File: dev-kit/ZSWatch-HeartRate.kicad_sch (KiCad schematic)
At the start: 49 parts, among them IC101 LIS2DS12, IC102 MCP73832-2-OT, IC103 MAX32664, IC104 TPS61240, IC105 MAX86141, IC106 MIC5365-1.8, J101 SPI, J102 GPIO, J103 UART, J104 I2C, M101 BM15C, SW101 BTN1, SW102 RESET, X102 CHARGE, X103 BATTERY, X104 DEBUG, Y101 32kHz

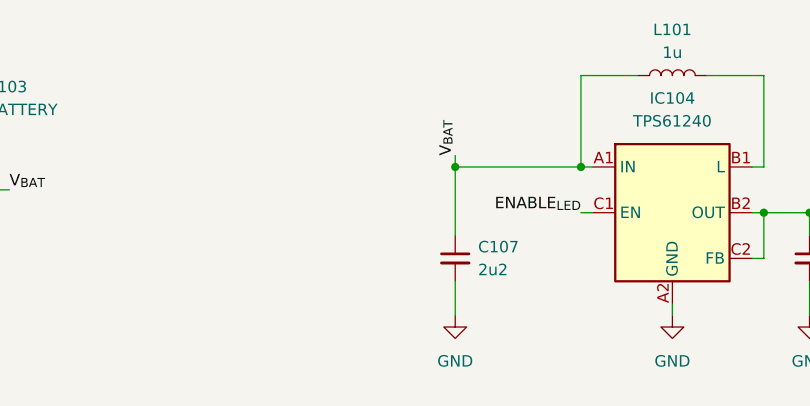
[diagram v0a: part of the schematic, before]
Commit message: Start with hardware rev 3
- Fix distance between programming and battery connector

Signed-off-by: Daniel Kampert <DanielKampert@kampis-elektroecke.de>
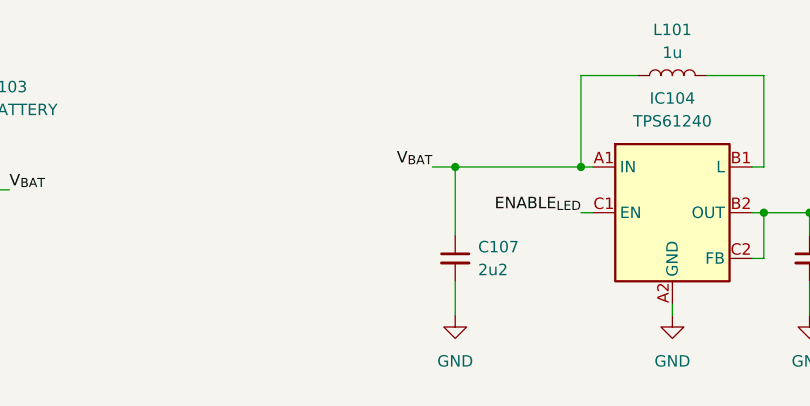
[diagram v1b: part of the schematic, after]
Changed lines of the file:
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@@
 	(title_block
 		(title "ZSWatch Heart Rate Dev-Board")
-		(date "2025-04-18")
-		(rev "2")
+		(date "2025-05-20")
+		(rev "3")
 		(company "github.com/...")
 	)
@@
 	(wire
 		(pts
+			(xy 353.06 30.48) (xy 355.6 30.48)
+		)
+		(stroke
+			(width 0)
+			(type default)
+		)
+	)
+	(wire
+		(pts
 			(xy 214.63 113.03) (xy 214.63 114.3)
 		)
@@
 	(wire
 		(pts
-			(xy 355.6 29.21) (xy 355.6 30.48)
-		)
-		(stroke
-			(width 0)
-			(type default)
-		)
-	)
-	(wire
-		(pts
 			(xy 222.25 40.64) (xy 222.25 39.37)
 		)
@@
 	)
 	(label "V_{BAT}"
-		(at 355.6 29.21 90)
+		(at 353.06 30.48 180)
 		(fields_autoplaced yes)
 		(effects
@@
 				(size 1.27 1.27)
 			)
-			(justify left bottom)
+			(justify right bottom)
 		)
 	)

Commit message: Switch to KiCad 9
Signed-off-by: Daniel Kampert <DanielKampert@kampis-elektroecke.de>
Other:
- company: github.com/... -> https://github.com/ZSWatch/Heartrate-HW
- title: ZSWatch Heart Rate Dev-Board -> Heart Rate Dev-Board
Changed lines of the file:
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@@
 (kicad_sch
-	(version 20231120)
+	(version 20250114)
 	(generator "eeschema")
-	(generator_version "8.0")
+	(generator_version "9.0")
 	(paper "A3")
 	(title_block
-		(title "ZSWatch Heart Rate Dev-Board")
-		(date "2025-05-20")
+		(title "Heart Rate Dev-Board")
+		(date "2025-07-29")
 		(rev "3")
-		(company "github.com/...")
+		(company "https://github.com/ZSWatch/Heartrate-HW")
+	)
+	(text "TODO: Can we use GPIO1 or 2 to Enable / Disable VLED?"
+		(exclude_from_sim no)
+		(at 369.824 180.848 0)
+		(effects
+			(font
+				(size 1.27 1.27)
+			)
+		)
+	)
+	(text "Layout guidelines for MAX8614x:\n- Connect all GNDs to a single ground plane and use one single via to PCB ground\n- Use different vias for all decoupling caps\n- PD_IN must be shielded by PD_GND\n- PD_GND on the layer where the MAX8614x is mounted, PG_IN under PD_GND\n- No traces over or under PD_GND"
+		(exclude_from_sim no)
+		(at 275.336 149.352 0)
+		(effects
+			(font
+				(size 1.27 1.27)
+			)
+			(justify left top)
+		)
+	)
+	(text "880 nm"
+		(exclude_from_sim no)
+		(at 352.552 104.394 0)
+		(effects
+			(font
+				(size 1.27 1.27)
+			)
+		)
+	)
+	(text "660 nm"
+		(exclude_from_sim no)
+		(at 374.015 104.14 0)
+		(effects
+			(font
+				(size 1.27 1.27)
+			)
+		)
+	)
+	(text "557 nm"
+		(exclude_from_sim no)
+		(at 329.692 104.394 0)
+		(effects
+			(font
+				(size 1.27 1.27)
+			)
+		)
 	)
 	(junction
@@
 		)
 	)
-	(text "TODO: Can we use GPIO1 or 2 to Enable / Disable VLED?"
-		(exclude_from_sim no)
-		(at 369.824 180.848 0)
-		(effects
-			(font
-				(size 1.27 1.27)
-			)
-		)
-	)
-	(text "Layout guidelines for MAX8614x:\n- Connect all GNDs to a single ground plane and use one single via to PCB ground\n- Use different vias for all decoupling caps\n- PD_IN must be shielded by PD_GND\n- PD_GND on the layer where the MAX8614x is mounted, PG_IN under PD_GND\n- No traces over or under PD_GND"
-		(exclude_from_sim no)
-		(at 275.336 149.352 0)
-		(effects
-			(font
-				(size 1.27 1.27)
-			)
-			(justify left top)
-		)
-	)
-	(text "880 nm"
-		(exclude_from_sim no)
-		(at 352.552 104.394 0)
-		(effects
-			(font
-				(size 1.27 1.27)
-			)
-		)
-	)
-	(text "660 nm"
-		(exclude_from_sim no)
-		(at 374.015 104.14 0)
-		(effects
-			(font
-				(size 1.27 1.27)
-			)
-		)
-	)
-	(text "557 nm"
-		(exclude_from_sim no)
-		(at 329.692 104.394 0)
-		(effects
-			(font
-				(size 1.27 1.27)
-			)
-		)
-	)
 	(label "~{RESET}"
 		(at 287.02 250.19 0)
-		(fields_autoplaced yes)
 		(effects
 			(font
@@
 	(label "V_{LED}"
 		(at 396.24 35.56 0)
-		(fields_autoplaced yes)
 		(effects
 			(font
@@
 	(label "SWDIO"
 		(at 287.02 257.81 0)
-		(fields_autoplaced yes)
 		(effects
 			(font
@@
 	(label "INT_{ACC}"
 		(at 316.23 205.74 0)
-		(fields_autoplaced yes)
 		(effects
 			(font
@@
 	(label "TxD"
 		(at 59.69 195.58 180)
-		(fields_autoplaced yes)
 		(effects
 			(font
@@
 	(label "~{RESET_{HR}}"
 		(at 115.57 217.17 0)
-		(fields_autoplaced yes)
 		(effects
 			(font
@@
 	(label "ENABLE_{LED}"
 		(at 369.57 35.56 180)
-		(fields_autoplaced yes)
 		(effects
 			(font
@@
 	(label "SDA"
 		(at 146.05 128.27 180)
-		(fields_autoplaced yes)
 		(effects
 			(font
@@
 	(label "INT_{ACC}"
 		(at 210.82 127 0)
-		(fields_autoplaced yes)
 		(effects
 			(font
@@
 	(label "V_{LED}"
 		(at 336.55 97.79 90)
-		(fields_autoplaced yes)
 		(effects
 			(font
@@
 	(label "CHARGE"
 		(at 275.59 38.1 0)
-		(fields_autoplaced yes)
 		(effects
 			(font
@@
 	(label "V_{LED}"
 		(at 292.1 77.47 90)
-		(fields_autoplaced yes)
 		(effects
 			(font
@@
 	(label "SWDCLK"
 		(at 287.02 255.27 0)
-		(fields_autoplaced yes)
 		(effects
 			(font
@@
 	(label "STATUS"
 		(at 115.57 219.71 0)
-		(fields_autoplaced yes)
 		(effects
 			(font
@@
 	(label "CHARGE"
 		(at 115.57 234.95 0)
-		(fields_autoplaced yes)
 		(effects
 			(font
@@
 	(label "V_{LED}"
 		(at 359.41 97.79 90)
-		(fields_autoplaced yes)
 		(effects
 			(font
@@
 	(label "V_{LED}"
 		(at 381 97.79 90)
-		(fields_autoplaced yes)
 		(effects
 			(font
@@
 	(label "V_{BAT}"
 		(at 353.06 30.48 180)
-		(fields_autoplaced yes)
 		(effects
 			(font
@@
 	(label "V_{BAT}"
 		(at 353.06 67.31 180)
-		(fields_autoplaced yes)
 		(effects
 			(font
@@
 	(label "SWDCLK"
 		(at 59.69 182.88 180)
-		(fields_autoplaced yes)
 		(effects
 			(font
@@
 	(label "STATUS"
 		(at 210.82 129.54 0)
-		(fields_autoplaced yes)
 		(effects
 			(font
@@
 	(label "SCL"
 		(at 115.57 237.49 0)
-		(fields_autoplaced yes)
 		(effects
 			(font
@@
 	(label "ENABLE_{LED}"
 		(at 134.62 232.41 0)
-		(fields_autoplaced yes)
 		(effects
 			(font
@@
 	(label "TxD"
 		(at 121.92 165.1 270)
-		(fields_autoplaced yes)
 		(effects
 			(font
@@
 	(label "SDA"
 		(at 115.57 242.57 0)
-		(fields_autoplaced yes)
 		(effects
 			(font
@@
 	(label "SWDIO"
 		(at 59.69 185.42 180)
-		(fields_autoplaced yes)
 		(effects
 			(font
@@
 	(label "SCL"
 		(at 146.05 130.81 180)
-		(fields_autoplaced yes)
 		(effects
 			(font
@@
 	(label "V_{BAT}"
 		(at 306.07 33.02 0)
-		(fields_autoplaced yes)
 		(effects
 			(font
@@
 	(label "~{RESET_{HR}}"
 		(at 146.05 123.19 180)
-		(fields_autoplaced yes)
 		(effects
 			(font
@@
 	(label "~{RESET}"
 		(at 31.75 176.53 180)
-		(fields_autoplaced yes)
 		(effects
 			(font
@@
 		)
 	)
+	(embedded_fonts no)
 )

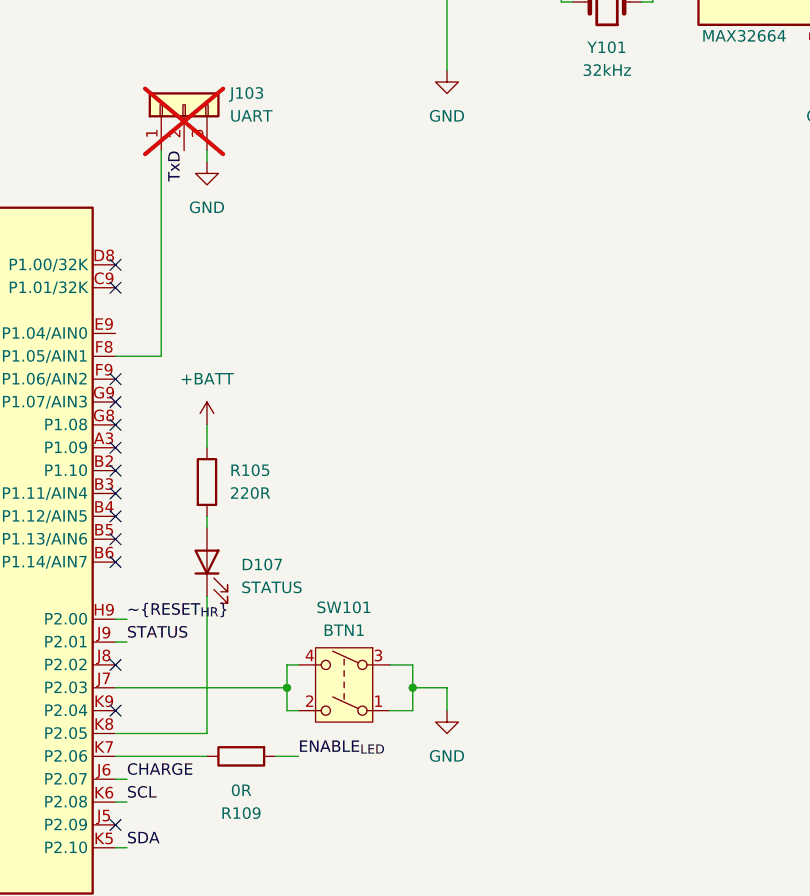
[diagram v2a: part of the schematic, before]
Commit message: Bug: Issue #2
- Fix wrong circuit for the status LED

Signed-off-by: Daniel Kampert <DanielKampert@kampis-elektroecke.de>
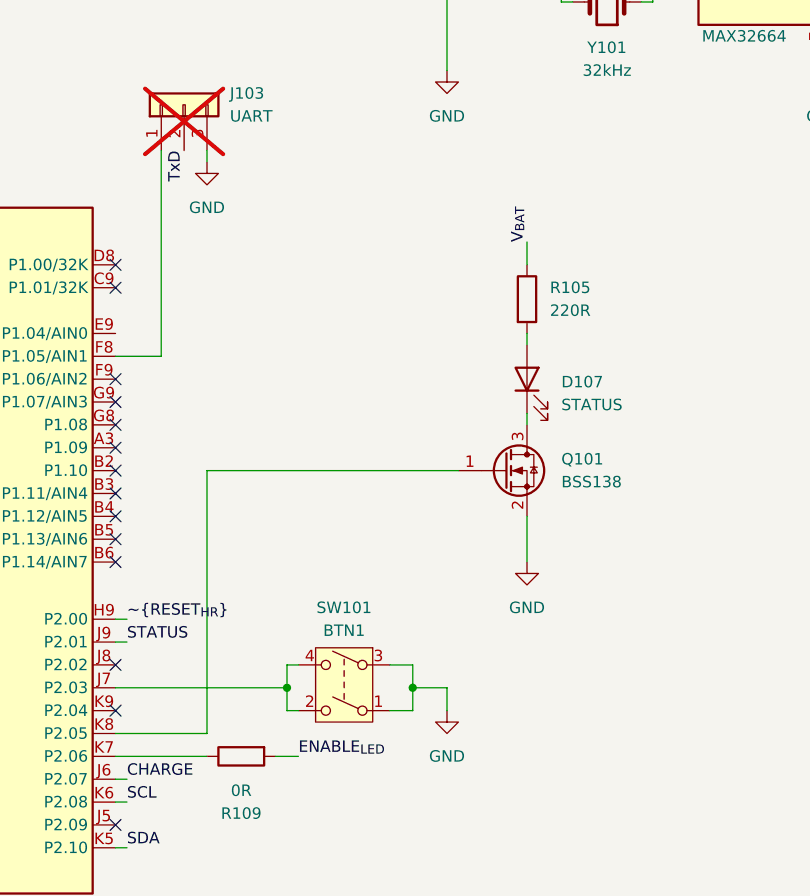
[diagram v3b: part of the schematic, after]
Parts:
- added Q101: BSS138, Package_TO_SOT_SMD:SOT-23, symbol Transistor_FET:BSS138
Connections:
- net +BATT is gone; now on net V_{BAT}: R105.1
- net GND: now also Q101.2 (S)
- net at D107.1 (K): now also Q101.3 (D); no longer M101.K8 (P2.05)
- new net: M101.K8 (P2.05), Q101.1 (G)
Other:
- moved on the sheet: D107, R105
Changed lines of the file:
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@@
 	(wire
 		(pts
+			(xy 124.46 200.66) (xy 152.4 200.66)
+		)
+		(stroke
+			(width 0)
+			(type default)
+		)
+	)
+	(wire
+		(pts
 			(xy 248.92 38.1) (xy 246.38 38.1)
 		)
@@
 	(wire
 		(pts
+			(xy 160.02 205.74) (xy 160.02 210.82)
+		)
+		(stroke
+			(width 0)
+			(type default)
+		)
+	)
+	(wire
+		(pts
 			(xy 48.26 176.53) (xy 38.1 176.53)
 		)
@@
 	(wire
 		(pts
-			(xy 124.46 205.74) (xy 124.46 207.01)
+			(xy 160.02 185.42) (xy 160.02 186.69)
 		)
 		(stroke
@@
 	(wire
 		(pts
+			(xy 124.46 200.66) (xy 124.46 229.87)
+		)
+		(stroke
+			(width 0)
+			(type default)
+		)
+	)
+	(wire
+		(pts
 			(xy 285.75 80.01) (xy 285.75 78.74)
 		)
@@
 	(wire
 		(pts
+			(xy 160.02 194.31) (xy 160.02 195.58)
+		)
+		(stroke
+			(width 0)
+			(type default)
+		)
+	)
+	(wire
+		(pts
 			(xy 146.05 128.27) (xy 156.21 128.27)
 		)
@@
 	(wire
 		(pts
-			(xy 124.46 195.58) (xy 124.46 198.12)
+			(xy 160.02 175.26) (xy 160.02 177.8)
 		)
 		(stroke
@@
 	(wire
 		(pts
-			(xy 124.46 214.63) (xy 124.46 229.87)
-		)
-		(stroke
-			(width 0)
-			(type default)
-		)
-	)
-	(wire
-		(pts
 			(xy 226.06 161.29) (xy 228.6 161.29)
 		)
@@
 	)
 	(label "V_{BAT}"
+		(at 160.02 175.26 90)
+		(effects
+			(font
+				(size 1.27 1.27)
+			)
+			(justify left bottom)
+		)
+	)
+	(label "V_{BAT}"
 		(at 306.07 33.02 0)
 		(effects
@@
 	)
 	(symbol
-		(lib_id "power:+BATT")
-		(at 124.46 195.58 0)
-		(unit 1)
-		(exclude_from_sim no)
-		(in_bom yes)
-		(on_board yes)
-		(dnp no)
-		(fields_autoplaced yes)
-		(property "Reference" "#PWR0101"
-			(at 124.46 199.39 0)
-			(effects
-				(font
-					(size 1.27 1.27)
-				)
-				(hide yes)
-			)
-		)
-		(property "Value" "+BATT"
-			(at 124.46 190.5 0)
-			(effects
-				(font
-					(size 1.27 1.27)
-				)
-			)
-		)
-		(property "Footprint" ""
-			(at 124.46 195.58 0)
-			(effects
-				(font
-					(size 1.27 1.27)
-				)
-				(hide yes)
-			)
-		)
-		(property "Datasheet" ""
-			(at 124.46 195.58 0)
-			(effects
-				(font
-					(size 1.27 1.27)
-				)
-				(hide yes)
-			)
-		)
-		(property "Description" "Power symbol creates a global label with name \"+BATT\""
-			(at 124.46 195.58 0)
-			(effects
-				(font
-					(size 1.27 1.27)
-				)
-				(hide yes)
-			)
-		)
-		(pin "1"
-		)
-		(instances
-			(project "ZSWatch-HeartRate"
-				(path "/d5742f03-3b1a-42e5-a384-018bd4b919aa"
-					(reference "#PWR0101")
-					(unit 1)
-				)
-			)
-		)
-	)
-	(symbol
 		(lib_id "Device:C_Small")
 		(at 91.44 160.02 0)
@@
 	(symbol
 		(lib_id "Device:R")
-		(at 124.46 201.93 0)
+		(at 160.02 181.61 0)
 		(unit 1)
 		(exclude_from_sim no)
@@
 		(fields_autoplaced yes)
 		(property "Reference" "R105"
-			(at 127 200.6599 0)
+			(at 162.56 180.3399 0)
 			(effects
 				(font
@@
 		)
 		(property "Value" "220R"
-			(at 127 203.1999 0)
+			(at 162.56 182.8799 0)
 			(effects
 				(font
@@
 		)
 		(property "Footprint" "Capacitor_SMD:C_0603_1608Metric"
-			(at 122.682 201.93 90)
+			(at 158.242 181.61 90)
 			(effects
 				(font
@@
 		)
 		(property "Datasheet" "https://www.mouser.de/datasheet/2/54/cr-1858361.pdf"
-			(at 124.46 201.93 0)
+			(at 160.02 181.61 0)
 			(effects
 				(font
@@
 		)
 		(property "Description" "Resistor"
-			(at 124.46 201.93 0)
+			(at 160.02 181.61 0)
 			(effects
 				(font
@@
 		)
 		(property "manf" "Bourns"
-			(at 124.46 201.93 0)
+			(at 160.02 181.61 0)
 			(effects
 				(font
@@
 		)
 		(property "manf#" "CR0402-JW-221GLF"
-			(at 124.46 201.93 0)
+			(at 160.02 181.61 0)
 			(effects
 				(font
@@
 		)
 		(property "mouser#" "652-CR0402-JW-221GLF"
-			(at 124.46 201.93 0)
+			(at 160.02 181.61 0)
 			(effects
 				(font
@@
 		)
 		(property "CONFIG" ""
-			(at 124.46 201.93 0)
+			(at 160.02 181.61 0)
 			(effects
 				(font
@@
 	(symbol
 		(lib_id "Device:LED")
-		(at 124.46 210.82 90)
+		(at 160.02 190.5 90)
 		(unit 1)
 		(exclude_from_sim no)
@@
 		(fields_autoplaced yes)
 		(property "Reference" "D107"
-			(at 128.27 211.1374 90)
+			(at 163.83 190.8174 90)
 			(effects
 				(font
@@
 		)
 		(property "Value" "STATUS"
-			(at 128.27 213.6774 90)
+			(at 163.83 193.3574 90)
 			(effects
 				(font
@@
 		)
 		(property "Footprint" "LED_SMD:LED_0805_2012Metric_Pad1.15x1.40mm_HandSolder"
-			(at 124.46 210.82 0)
+			(at 160.02 190.5 0)
 			(effects
 				(font
@@
 		)
 		(property "Datasheet" "https://www.mouser.de/datasheet/2/678/hsmq_c170_t0000_ds100-2498198.pdf"
-			(at 124.46 210.82 0)
+			(at 160.02 190.5 0)
 			(effects
 				(font
@@
 		)
 		(property "Description" "Light emitting diode"
-			(at 124.46 210.82 0)
+			(at 160.02 190.5 0)
 			(effects
 				(font
@@
 		)
 		(property "manf" "Broadcom / Avago"
-			(at 124.46 210.82 0)
+			(at 160.02 190.5 0)
 			(effects
 				(font
@@
 		)
 		(property "manf#" "HSMQ-C170-T0000"
-			(at 124.46 210.82 0)
+			(at 160.02 190.5 0)
 			(effects
 				(font
@@
 		)
 		(property "mouser#" "630-HSMQ-C170-T0000"
-			(at 124.46 210.82 0)
+			(at 160.02 190.5 0)
 			(effects
 				(font
@@
 		)
 		(property "CONFIG" ""
-			(at 124.46 210.82 0)
+			(at 160.02 190.5 0)
 			(effects
 				(font
@@
 	(symbol
 		(lib_id "power:GND")
+		(at 160.02 210.82 0)
+		(mirror y)
+		(unit 1)
+		(exclude_from_sim no)
+		(in_bom yes)
+		(on_board yes)
+		(dnp no)
+		(property "Reference" "#PWR0152"
+			(at 160.02 217.17 0)
+			(effects
+				(font
+					(size 1.27 1.27)
+				)
+				(hide yes)
+			)
+		)
+		(property "Value" "GND"
+			(at 160.02 215.9 0)
+			(effects
+				(font
+					(size 1.27 1.27)
+				)
+			)
+		)
+		(property "Footprint" ""
+			(at 160.02 210.82 0)
+			(effects
+				(font
+					(size 1.27 1.27)
+				)
+				(hide yes)
+			)
+		)
+		(property "Datasheet" ""
+			(at 160.02 210.82 0)
+			(effects
+				(font
+					(size 1.27 1.27)
+				)
+				(hide yes)
+			)
+		)
+		(property "Description" "Power symbol creates a global label with name \"GND\" , ground"
+			(at 160.02 210.82 0)
+			(effects
+				(font
+					(size 1.27 1.27)
+				)
+				(hide yes)
+			)
+		)
+		(pin "1"
+		)
+		(instances
+			(project "ZSWatch-HeartRate"
+				(path "/d5742f03-3b1a-42e5-a384-018bd4b919aa"
+					(reference "#PWR0152")
+					(unit 1)
+				)
+			)
+		)
+	)
+	(symbol
+		(lib_id "power:GND")
 		(at 227.33 175.26 0)
 		(mirror y)
@@
 					(unit 1)
 				)
+			)
+		)
+	)
+	(symbol
+		(lib_id "Transistor_FET:BSS138")
+		(at 157.48 200.66 0)
+		(unit 1)
+		(exclude_from_sim no)
+		(in_bom yes)
+		(on_board yes)
+		(dnp no)
+		(fields_autoplaced yes)
+		(property "Reference" "Q101"
+			(at 163.83 199.3899 0)
+			(effects
+				(font
+					(size 1.27 1.27)
+				)
+				(justify left)
+			)
+		)
+		(property "Value" "BSS138"
+			(at 163.83 201.9299 0)
+			(effects
+				(font
+					(size 1.27 1.27)
+				)
+				(justify left)
+			)
+		)
+		(property "Footprint" "Package_TO_SOT_SMD:SOT-23"
+			(at 162.56 202.565 0)
+			(effects
+				(font
+					(size 1.27 1.27)
+					(italic yes)
+				)
+				(justify left)
+				(hide yes)
+			)
+		)
+		(property "Datasheet" "https://www.onsemi.com/pub/Collateral/BSS138-D.PDF"
+			(at 162.56 204.47 0)
+			(effects
+				(font
+					(size 1.27 1.27)
+				)
+				(justify left)
+				(hide yes)
+			)
+		)
+		(property "Description" "50V Vds, 0.22A Id, N-Channel MOSFET, SOT-23"
+			(at 157.48 200.66 0)
+			(effects
+				(font
+					(size 1.27 1.27)
+				)
+				(hide yes)
+			)
+		)
+		(property "manf" "onsemi / Fairchild"
+			(at 157.48 200.66 0)
+			(effects
+				(font
+					(size 1.27 1.27)
+				)
+				(hide yes)
+			)
+		)
+		(property "manf#" "BSS138"
+			(at 157.48 200.66 0)
+			(effects
+				(font
+					(size 1.27 1.27)
+				)
+				(hide yes)
+			)
+		)
+		(property "mouser#" "512-BSS138"
+			(at 157.48 200.66 0)
+			(effects
+				(font
+					(size 1.27 1.27)
+				)
+				(hide yes)
+			)
+		)
+		(pin "3"
+		)
+		(pin "1"
+		)
+		(pin "2"
+		)
+		(instances
+			(project ""
+				(path "/d5742f03-3b1a-42e5-a384-018bd4b919aa"
+					(reference "Q101")
+					(unit 1)
+				)
